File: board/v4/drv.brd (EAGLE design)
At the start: 34 x 30 mm, 12 parts, among them IC1 TINY24/44/84-SSU, J1 22-27-2031-03

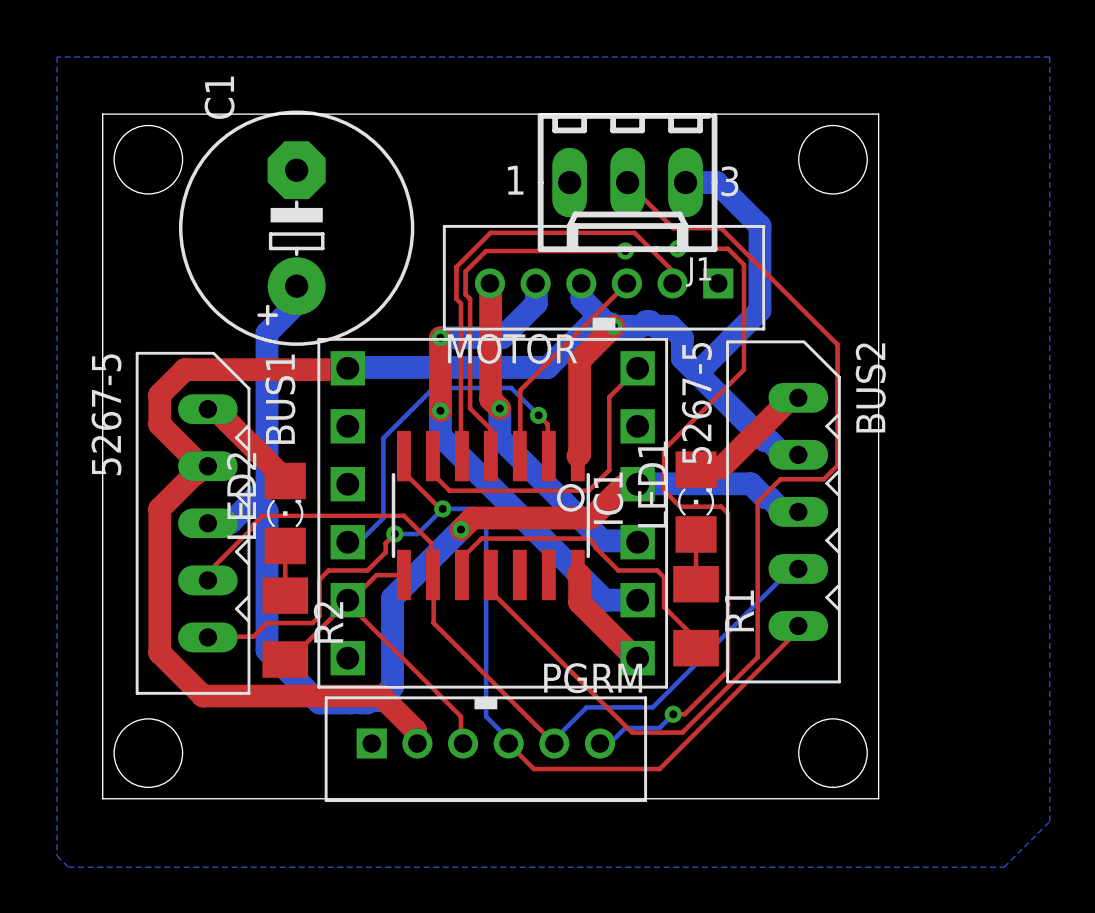
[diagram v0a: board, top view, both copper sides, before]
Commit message: Change computers
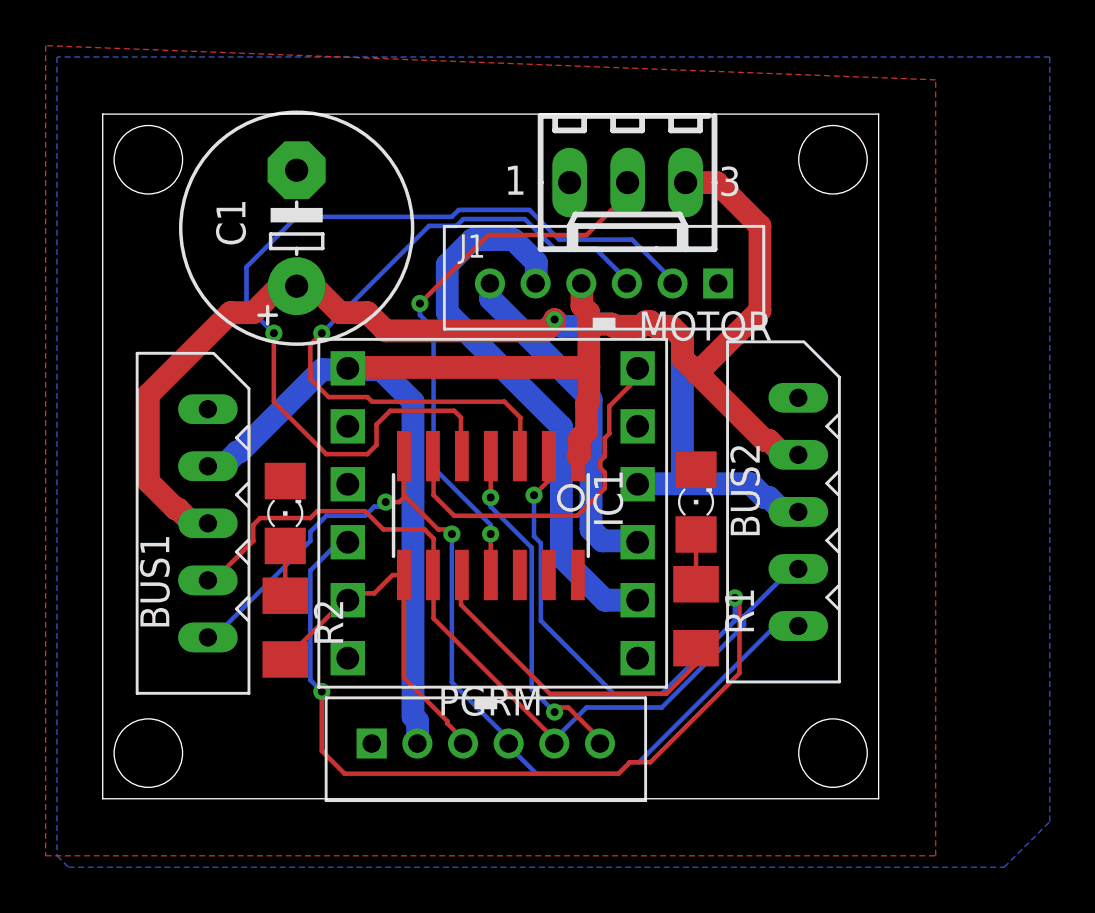
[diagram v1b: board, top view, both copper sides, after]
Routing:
- net DIR: track 15.7 -> 54.0 mm, vias 1 -> 3
- net RESET: track 49.9 -> 15.2 mm, vias 3 -> 2
- net ENC2: track 9.50 -> 30.5 mm, vias 0 -> 1
- net ENC1: track 19.7 -> 39.8 mm, vias 0 -> 1
- net SENSOR1: track 44.8 -> 24.8 mm, vias 0 -> 2
- net GND: track 15.4 -> 0.00 mm
- net 5V: track 78.9 -> 68.8 mm, vias 1 -> 0
- net M1: track 21.6 -> 24.7 mm, vias 2 -> 0
- net SDA/MOSI: track 44.9 -> 42.2 mm
- net 12V: track 50.5 -> 48.2 mm
- net FAULT: track 14.2 -> 16.1 mm
- net CLKS: track 36.8 -> 37.5 mm
- net M2: vias 1 -> 0
- added copper zone on layer 1, net GND
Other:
- board text added: "GND"
